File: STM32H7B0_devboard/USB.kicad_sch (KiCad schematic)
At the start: 7 parts, among them P1 USB_C, U2 USBLC6-2SC6

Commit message: Schematic done!
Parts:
- removed P1: USB_C, symbol Connector:USB_C_Plug_USB2.0
- removed R1, R5: 22, symbol Device:R_Small
- removed R7: 5k1, symbol Device:R_Small
- added J3: USB-C 16P, Connector_USB:USB_C_Receptacle_HCTL_HC-TYPE-C-16P-01A, symbol Connector:USB_C_Receptacle_USB2.0_16P
- FL1: value 0603USB-222 -> TDK ACM2012-900; footprint Inductor_SMD:L_CommonModeChoke_Coilcraft_0603USB -> (none)
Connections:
- net GND: now also J3.A1 (GND), J3.A12 (GND), J3.B1 (GND), J3.B12 (GND)
- net USB_DM: now also FL1.2
- net USB_DP: now also FL1.3
- net VBUS: now also J3.A4 (VBUS), J3.A9 (VBUS), J3.B4 (VBUS), J3.B9 (VBUS)
- net at U2.1 (I/O1): now also J3.A7 (D-), J3.B7 (D-)
- net at U2.3 (I/O2): now also J3.A6 (D+), J3.B6 (D+)
- net CC2: no longer names the net of R6.2
- net CC2: now also J3.A5 (CC1), J3.B5 (CC2)
- no-connect marks 0 -> 3
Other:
- note added: "CC1"
- note added: "CC2"
- note removed: "TODO: chocke valid use USB common mode chocke (O805USB-902ML) ??"
- moved on the sheet: FL1, R6, U2

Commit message: Breakout
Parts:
- FL1: footprint (none) -> ACM2012_900_2P_T002:ACM2012_TDK
- renumbered R6 to R22, U2 to U5
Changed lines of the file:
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@@
 		(on_board yes)
 		(dnp no)
-		(property "Reference" "#PWR019"
+		(property "Reference" "#PWR046"
 			(at 30.48 67.31 0)
 			(effects
@@
 			(project "STM32H7B0_devboard"
 				(path "/0c02ba0f-c40f-484f-a270-dfb4a249f2e6/b477b51e-f069-4c33-a922-9557e4b10dad"
-					(reference "#PWR019")
+					(reference "#PWR046")
 					(unit 1)
 				)
@@
 		(on_board yes)
 		(dnp no)
-		(property "Reference" "U2"
+		(property "Reference" "U5"
 			(at 66.294 32.766 0)
 			(effects
@@
 			(project "STM32H7B0_devboard"
 				(path "/0c02ba0f-c40f-484f-a270-dfb4a249f2e6/b477b51e-f069-4c33-a922-9557e4b10dad"
-					(reference "U2")
+					(reference "U5")
 					(unit 1)
 				)
@@
 		(on_board yes)
 		(dnp no)
-		(property "Reference" "#PWR023"
+		(property "Reference" "#PWR044"
 			(at 55.88 34.29 0)
 			(effects
@@
 			(project "STM32H7B0_devboard"
 				(path "/0c02ba0f-c40f-484f-a270-dfb4a249f2e6/b477b51e-f069-4c33-a922-9557e4b10dad"
-					(reference "#PWR023")
+					(reference "#PWR044")
 					(unit 1)
 				)
@@
 			)
 		)
-		(property "Footprint" ""
+		(property "Footprint" "ACM2012_900_2P_T002:ACM2012_TDK"
 			(at 78.74 44.45 0)
 			(effects
@@
 		(on_board yes)
 		(dnp no)
-		(property "Reference" "#PWR020"
+		(property "Reference" "#PWR045"
 			(at 66.04 50.8 0)
 			(effects
@@
 			(project "STM32H7B0_devboard"
 				(path "/0c02ba0f-c40f-484f-a270-dfb4a249f2e6/b477b51e-f069-4c33-a922-9557e4b10dad"
-					(reference "#PWR020")
+					(reference "#PWR045")
 					(unit 1)
 				)
@@
 		(on_board yes)
 		(dnp no)
-		(property "Reference" "R6"
+		(property "Reference" "R22"
 			(at 51.054 25.908 90)
 			(effects
@@
 			(project "STM32H7B0_devboard"
 				(path "/0c02ba0f-c40f-484f-a270-dfb4a249f2e6/b477b51e-f069-4c33-a922-9557e4b10dad"
-					(reference "R6")
-					(unit 1)
-				)
+					(reference "R22")
+					(unit 1)
+				)

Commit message: Schematic V2.0 + Footprints
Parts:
- R22: footprint (none) -> Resistor_SMD:R_0402_1005Metric
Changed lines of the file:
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@@
 			)
 		)
-		(property "Footprint" ""
+		(property "Footprint" "Resistor_SMD:R_0402_1005Metric"
 			(at 50.8 27.94 0)
 			(effects

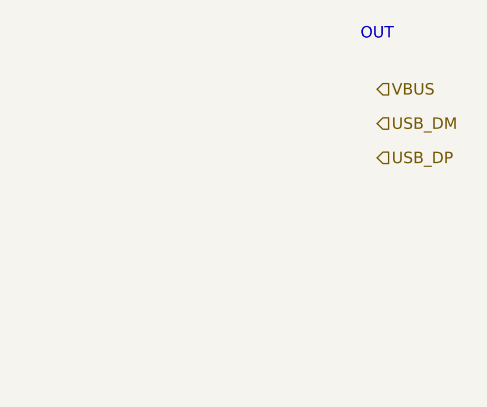
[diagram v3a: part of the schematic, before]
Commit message: Updated .gitignore
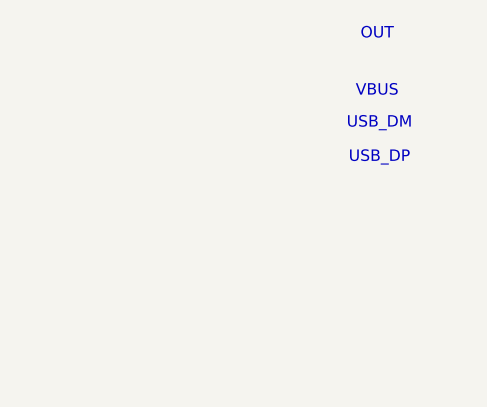
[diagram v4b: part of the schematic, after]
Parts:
- R22: footprint Resistor_SMD:R_0402_1005Metric -> Resistor_SMD:R_0603_1608Metric
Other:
- note added: "USB_DM"
- note added: "USB_DP"
- note added: "VBUS"
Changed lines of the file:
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@@
+		)
+	)
+	(text "USB_DM"
+		(exclude_from_sim no)
+		(at 260.604 29.21 0)
+		(effects
+			(font
+				(size 1.27 1.27)
+			)
+		)
+	)
+	(text "USB_DP"
+		(exclude_from_sim no)
+		(at 260.604 33.02 0)
+		(effects
+			(font
+				(size 1.27 1.27)
+			)
+		)
+	)
+	(text "VBUS"
+		(exclude_from_sim no)
+		(at 260.35 25.654 0)
+		(effects
+			(font
+				(size 1.27 1.27)
+			)
 		)
 	)
@@
 				(size 1.27 1.27)
 			)
-		)
-	)
-	(hierarchical_label "VBUS"
-		(shape input)
-		(at 260.35 25.4 0)
-		(fields_autoplaced yes)
-		(effects
-			(font
-				(size 1.27 1.27)
-			)
-			(justify left)
 		)
 	)
@@
 		)
 	)
-	(hierarchical_label "USB_DM"
-		(shape input)
-		(at 260.35 29.21 0)
-		(fields_autoplaced yes)
-		(effects
-			(font
-				(size 1.27 1.27)
-			)
-			(justify left)
-		)
-	)
 	(hierarchical_label "VBUS"
 		(shape input)
 		(at 69.85 22.86 0)
-		(fields_autoplaced yes)
-		(effects
-			(font
-				(size 1.27 1.27)
-			)
-			(justify left)
-		)
-	)
-	(hierarchical_label "USB_DP"
-		(shape input)
-		(at 260.35 33.02 0)
 		(fields_autoplaced yes)
 		(effects
@@
 			)
 		)
-		(property "Footprint" "Resistor_SMD:R_0402_1005Metric"
+		(property "Footprint" "Resistor_SMD:R_0603_1608Metric"
 			(at 50.8 27.94 0)
 			(effects

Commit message: Routing progress
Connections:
- net USB_DM renamed USB_DN
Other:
- note added: "USB_DN"
- note removed: "USB_DM"
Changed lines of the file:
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@@
 		)
 	)
-	(text "USB_DM"
+	(text "USB_DN"
 		(exclude_from_sim no)
 		(at 260.604 29.21 0)
@@
 		)
 	)
-	(hierarchical_label "USB_DM"
+	(hierarchical_label "USB_DN"
 		(shape input)
 		(at 88.9 35.56 0)

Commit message: Done V1
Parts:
- FL1: LCSC (none) -> C19972
- J3: LCSC (none) -> C2765186
- R22: LCSC (none) -> C26000
- U5: LCSC (none) -> C2827654
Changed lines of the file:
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@@
+			)
+		)
+		(property "LCSC" "C2827654"
+			(at 66.04 36.83 0)
+			(effects
+				(font
+					(size 1.27 1.27)
+				)
+				(hide yes)
 			)
 		)
@@
 			)
 		)
+		(property "LCSC" "C19972"
+			(at 78.74 38.1 0)
+			(effects
+				(font
+					(size 1.27 1.27)
+				)
+				(hide yes)
+			)
+		)
 		(pin "1"
 		)
@@
 			)
 		)
+		(property "LCSC" "C26000"
+			(at 50.8 27.94 0)
+			(effects
+				(font
+					(size 1.27 1.27)
+				)
+				(hide yes)
+			)
+		)
 		(pin "1"
 		)
@@
 			(at 30.48 38.1 0)
 			(effects
+				(font
+					(size 1.27 1.27)
+				)
+				(hide yes)
+			)
+		)
+		(property "LCSC" "C2765186"
+			(at 30.48 38.1 0)
+			(effects

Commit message: Finished board
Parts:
- J3: now not fitted
- R22: LCSC C26000 -> C23186
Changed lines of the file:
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@@
 			)
 		)
-		(property "LCSC" "C26000"
+		(property "LCSC" "C23186"
 			(at 50.8 27.94 0)
 			(effects
@@
 		(in_bom yes)
 		(on_board yes)
-		(dnp no)
+		(dnp yes)
 		(property "Reference" "J3"
 			(at 39.37 18.796 0)
